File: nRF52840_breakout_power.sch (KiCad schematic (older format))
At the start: 18 parts, among them J6 S2B-PH-SM4-TB(LF)(SN), U2 BQ24072, U3 TPS63031

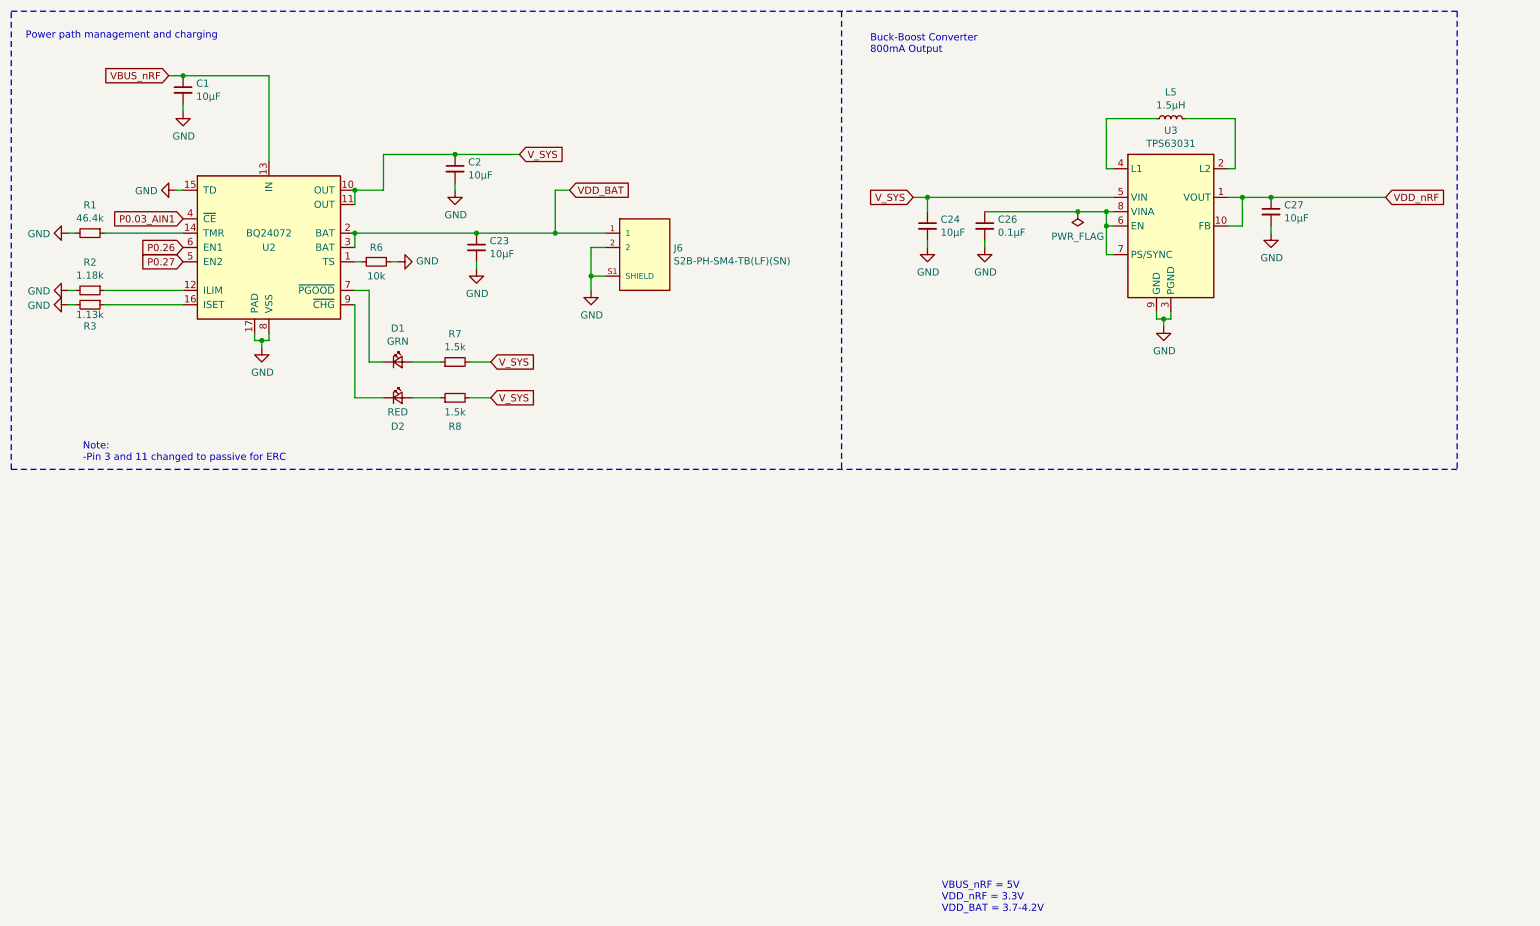
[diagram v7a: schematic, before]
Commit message: different power path management / got rid of var components
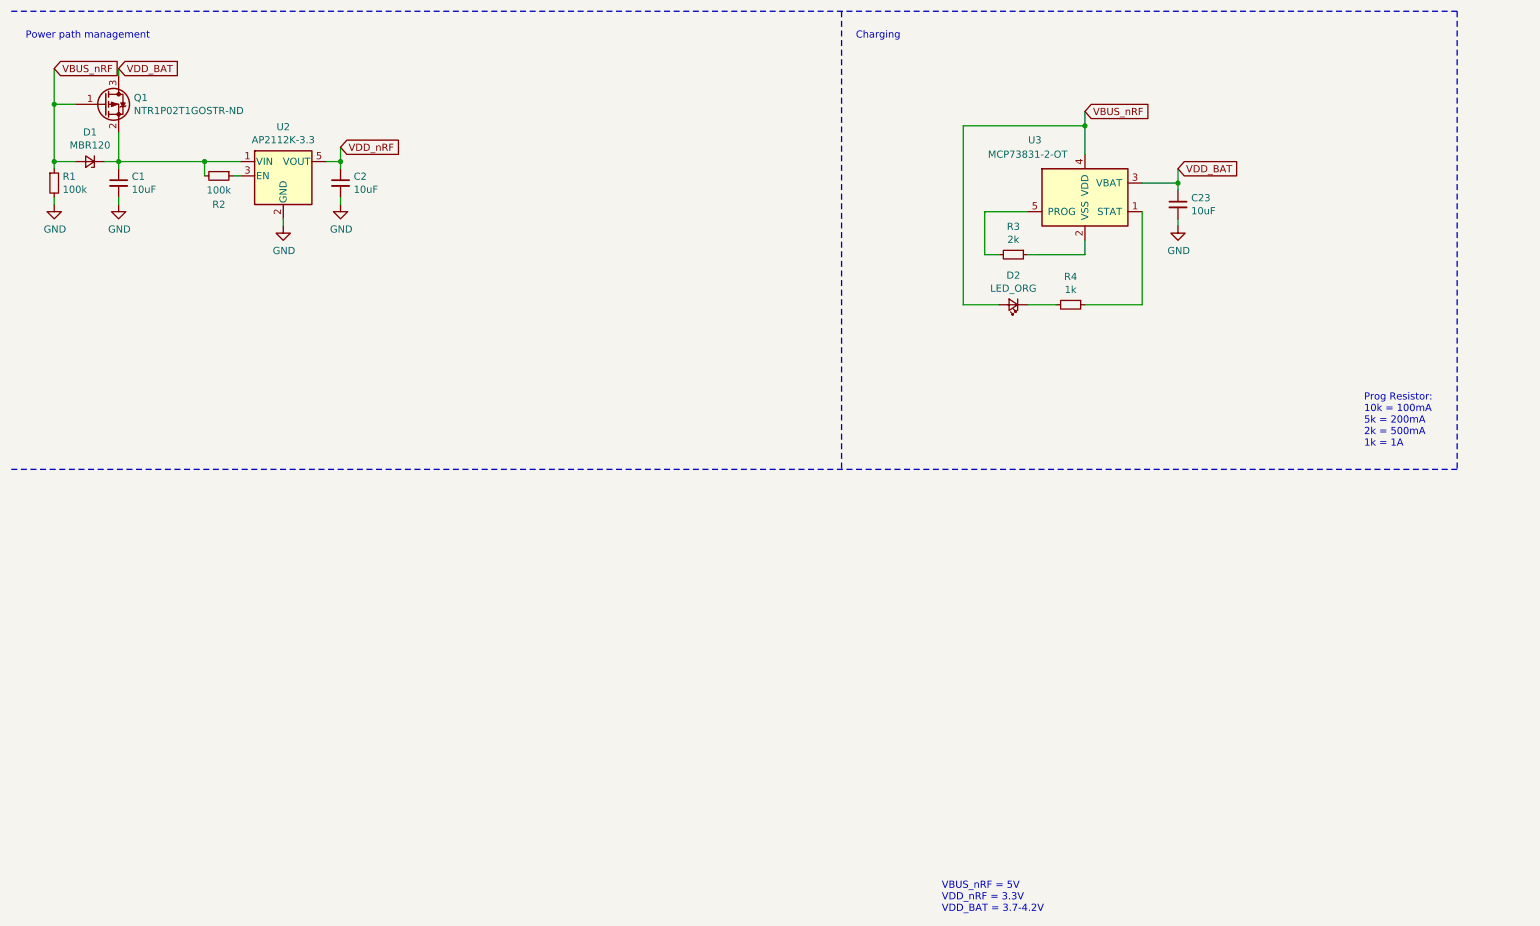
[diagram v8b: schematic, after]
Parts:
- removed C24, C27: 10µF, Capacitor_SMD:C_0402_1005Metric, symbol Device:C_Small
- removed C26: 0.1µF, Capacitor_SMD:C_0402_1005Metric, symbol Device:C_Small
- removed D1: GRN, LED_SMD:LED_0402_1005Metric, symbol Device:LED_Small
- removed J6: S2B-PH-SM4-TB(LF)(SN), custom_footprints:JST_PH_S2B-PH-SM4-TB_LF__SN_, symbol JST_PH_S2B-PH-SM4-TB_LF__SN_:S2B-PH-SM4-TB(LF)(SN)
- removed L5: 1.5µH, Inductor_SMD:L_0402_1005Metric, symbol Device:L_Small
- removed R6: 10k, Resistor_SMD:R_0402_1005Metric, symbol Device:R_Small
- removed R7, R8: 1.5k, Resistor_SMD:R_0402_1005Metric, symbol Device:R_Small
- removed U2: BQ24072, Package_DFN_QFN:VQFN-16-1EP_3x3mm_P0.5mm_EP1.68x1.68mm_ThermalVias, symbol BQ24072:BQ24072
- removed U3: TPS63031, Package_SON:Texas_DRC0010J_ThermalVias, symbol tps63031:TPS63031
- added D1: MBR120, Diode_SMD:D_SOD-123, symbol Device:D_Zener_Small
- added Q1: NTR1P02T1GOSTR-ND, Package_TO_SOT_SMD:SOT-23, symbol Device:Q_PMOS_GSD
- added R4: 1k, Resistor_SMD:R_0402_1005Metric, symbol Device:R_Small
- added U2: AP2112K-3.3, Package_TO_SOT_SMD:SOT-23-5, symbol Regulator_Linear:AP2112K-3.3
- added U3: MCP73831-2-OT, Package_TO_SOT_SMD:SOT-23-5, symbol Battery_Management:MCP73831-2-OT
- C1, C2, C23: value 10µF -> 10uF
- D2: value RED -> LED_ORG; footprint LED_SMD:LED_0402_1005Metric -> LED_SMD:LED_0603_1608Metric; Digikey (none) -> 160-1445-2-ND; MFG P/N (none) -> LTST-C191KFKT
- R1: value 46.4k -> 100k
- R2: value 1.18k -> 100k
- R3: value 1.13k -> 2k
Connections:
- net V_SYS is gone; now on net VDD_nRF: C2.1
- net GND: now also U2.2 (GND); no longer R2.2, R3.2
- net VBUS_nRF: now also D2.2 (A), R1.1, D1.2 (A), Q1.1 (G), U3.4 (VDD); no longer C1.1
- net VDD_BAT: now also Q1.3 (D), U3.3 (VBAT)
- net VDD_nRF: now also U2.5 (VOUT)
- net at R2.1: now also U2.3 (EN)
- net at R3.1: now also U3.2 (VSS)
- net at D2.1 (K): now also R4.2
- new net: C1.1, D1.1 (K), Q1.2 (S), R2.2, U2.1 (VIN)
- new net: R4.1, U3.1 (STAT)
- new net: R3.2, U3.5 (PROG)
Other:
- note added: "Charging"
- note added: "Power path management"
- note added: "Prog Resistor:\n10k = 100mA\n5k = 200mA\n2k = 500mA\n1k = 1A"
- note removed: "Buck-Boost Converter\n800mA Output"
- note removed: "Note:\n-Pin 3 and 11 changed to passive for ERC"
- note removed: "Power path management and charging"
